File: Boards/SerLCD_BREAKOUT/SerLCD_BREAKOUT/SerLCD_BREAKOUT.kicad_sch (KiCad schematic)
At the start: 2 parts, among them U1 SerLCD, U2 Teensy4.1_DEV-16771

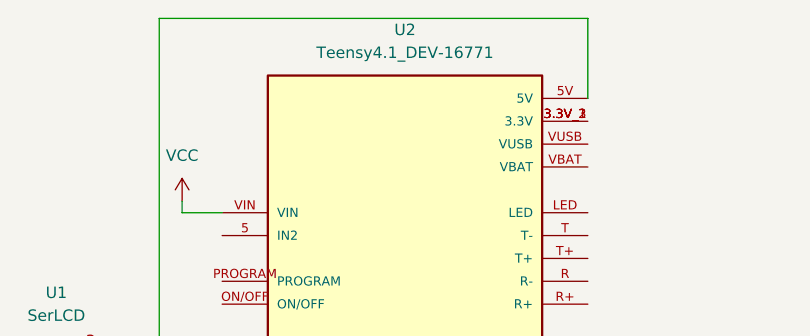
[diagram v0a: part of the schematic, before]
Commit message: Research Library Updates
Copied over MRDT footprints, symbols, and 3D models to Research Library
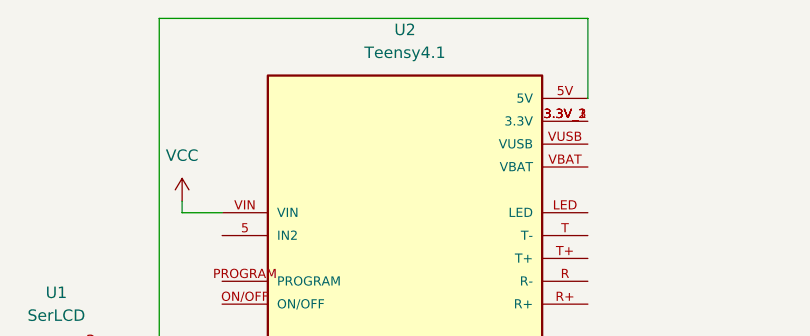
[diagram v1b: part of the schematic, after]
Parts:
- removed U2: Teensy4.1_DEV-16771, MRDT_Shields:MODULE_DEV-16771, symbol MRDT_Shields:Teensy4.1_DEV-16771
- added U2: Teensy4.1, MODULE_DEV-16771, symbol MRDT_Research:Teensy4.1
- U1: footprint MRDT_Connectors:MOLEX_SL_03_Vertical -> MRDT_Research:MOLEX_SL_03_Vertical
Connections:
- net GND: now also U2.GND1 (GND), U2.GND2 (GND), U2.GND3 (GND), U2.GND4 (GND), U2.GND5 (GND), U2.USB_GND1 (USB_GND), U2.USB_GND2 (USB_GND)
- net VCC: now also U2.VIN
- net at U1.3 (RX): now also U2.0 (RX1)
- net at U1.1 (Vcc): now also U2.5V
- new net: U2.3.3V_1 (3.3V), U2.3.3V_2 (3.3V), U2.3.3V_3 (3.3V)
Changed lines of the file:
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@@
     (pin "1")
   )
-  (symbol (lib_id "power:GND") (at 92.075 128.27 0) (unit 1)
-    (in_bom yes) (on_board yes)
-    (property "Reference" "#PWR0102" (id 0) (at 92.075 134.62 0)
-      (effects (font (size 1.27 1.27)) hide)
-    )
-    (property "Value" "GND" (id 1) (at 92.075 132.08 0))
-    (property "Footprint" "" (id 2) (at 92.075 128.27 0)
-      (effects (font (size 1.27 1.27)) hide)
-    )
-    (property "Datasheet" "" (id 3) (at 92.075 128.27 0)
-      (effects (font (size 1.27 1.27)) hide)
-    )
-    (pin "1")
-  )
-  (symbol (lib_id "power:GND") (at 38.1 62.865 0) (unit 1)
-    (in_bom yes) (on_board yes)
-    (property "Reference" "#PWR0101" (id 0) (at 38.1 69.215 0)
-      (effects (font (size 1.27 1.27)) hide)
-    )
-    (property "Value" "GND" (id 1) (at 38.1 66.675 0))
-    (property "Footprint" "" (id 2) (at 38.1 62.865 0)
-      (effects (font (size 1.27 1.27)) hide)
-    )
-    (property "Datasheet" "" (id 3) (at 38.1 62.865 0)
-      (effects (font (size 1.27 1.27)) hide)
-    )
-    (pin "1")
-  )
-  (symbol (lib_id "MRDT_Shields:Teensy4.1_DEV-16771") (at 67.945 78.74 0) (unit 1)
+  (symbol (lib_id "MRDT_Research:Teensy4.1") (at 67.945 78.74 0) (unit 1)
     (in_bom yes) (on_board yes) (fields_autoplaced)
     (property "Reference" "U2" (id 0) (at 67.945 22.86 0))
-    (property "Value" "Teensy4.1_DEV-16771" (id 1) (at 67.945 25.4 0))
-    (property "Footprint" "MRDT_Shields:MODULE_DEV-16771" (id 2) (at 121.285 86.36 0)
+    (property "Value" "Teensy4.1" (id 1) (at 67.945 25.4 0))
+    (property "Footprint" "MODULE_DEV-16771" (id 2) (at 121.285 86.36 0)
       (effects (font (size 1.27 1.27)) (justify left bottom) hide)
     )
@@
     (pin "VUSB")
   )
+  (symbol (lib_id "power:GND") (at 92.075 128.27 0) (unit 1)
+    (in_bom yes) (on_board yes)
+    (property "Reference" "#PWR0102" (id 0) (at 92.075 134.62 0)
+      (effects (font (size 1.27 1.27)) hide)
+    )
+    (property "Value" "GND" (id 1) (at 92.075 132.08 0))
+    (property "Footprint" "" (id 2) (at 92.075 128.27 0)
+      (effects (font (size 1.27 1.27)) hide)
+    )
+    (property "Datasheet" "" (id 3) (at 92.075 128.27 0)
+      (effects (font (size 1.27 1.27)) hide)
+    )
+    (pin "1")
+  )
+  (symbol (lib_id "power:GND") (at 38.1 62.865 0) (unit 1)
+    (in_bom yes) (on_board yes)
+    (property "Reference" "#PWR0101" (id 0) (at 38.1 69.215 0)
+      (effects (font (size 1.27 1.27)) hide)
+    )
+    (property "Value" "GND" (id 1) (at 38.1 66.675 0))
+    (property "Footprint" "" (id 2) (at 38.1 62.865 0)
+      (effects (font (size 1.27 1.27)) hide)
+    )
+    (property "Datasheet" "" (id 3) (at 38.1 62.865 0)
+      (effects (font (size 1.27 1.27)) hide)
+    )
+    (pin "1")
+  )
   (symbol (lib_id "MRDT_Research:SerLCD") (at 31.75 60.96 90) (unit 1)
     (in_bom yes) (on_board yes) (fields_autoplaced)
     (property "Reference" "U1" (id 0) (at 29.21 52.07 90))
     (property "Value" "SerLCD" (id 1) (at 29.21 54.61 90))
-    (property "Footprint" "MRDT_Connectors:MOLEX_SL_03_Vertical" (id 2) (at 31.75 60.96 0)
+    (property "Footprint" "MRDT_Research:MOLEX_SL_03_Vertical" (id 2) (at 31.75 60.96 0)
       (effects (font (size 1.27 1.27)) hide)
     )
@@
     )
     (path "/ef0beab9-973f-489d-b14b-402c1df9606c"
-      (reference "U1") (unit 1) (value "SerLCD") (footprint "MRDT_Connectors:MOLEX_SL_03_Vertical")
+      (reference "U1") (unit 1) (value "SerLCD") (footprint "MRDT_Research:MOLEX_SL_03_Vertical")
     )
-    (path "/e7ba0631-8a32-4cf8-b1e0-7389be80c395"
-      (reference "U2") (unit 1) (value "Teensy4.1_DEV-16771") (footprint "MRDT_Shields:MODULE_DEV-16771")
+    (path "/495f5c9d-290d-400c-acf8-7c17caa9c003"
+      (reference "U2") (unit 1) (value "Teensy4.1") (footprint "MRDT_Research:Teensy 4.1")
     )
   )
